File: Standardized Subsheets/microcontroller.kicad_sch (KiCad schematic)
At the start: 62 parts, among them J1 Conn_01x02, J2 Conn_01x02, J3 SWD, SW1 SW_SPDT, U1 STM32F105RCTx, U2 SN65HVD230, U3 SN65HVD230, Y1 16MHz

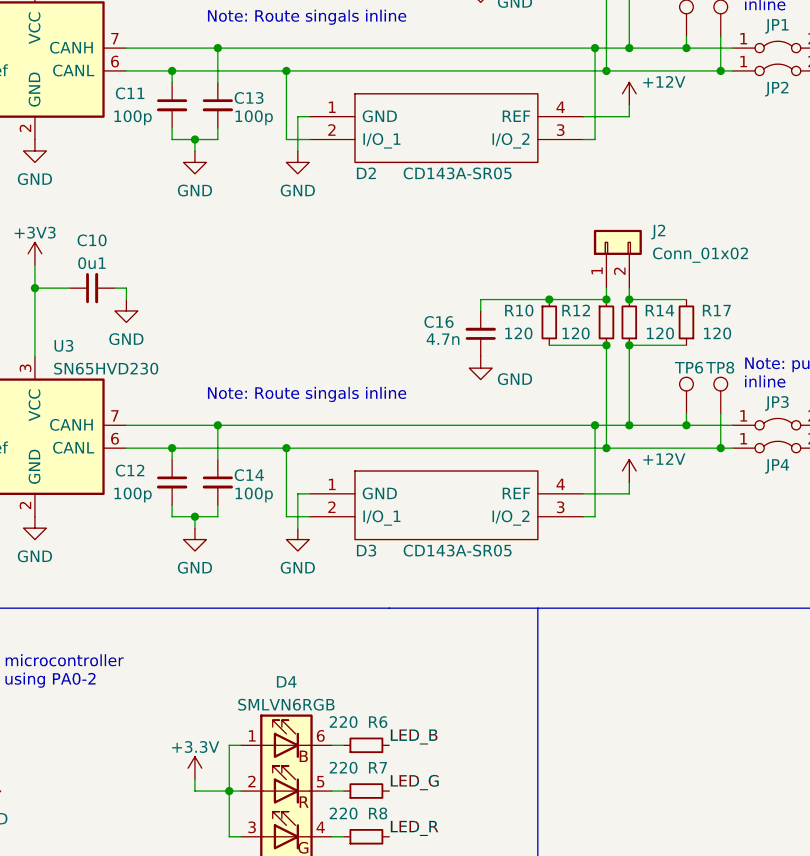
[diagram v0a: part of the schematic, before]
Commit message: updated connector footprint
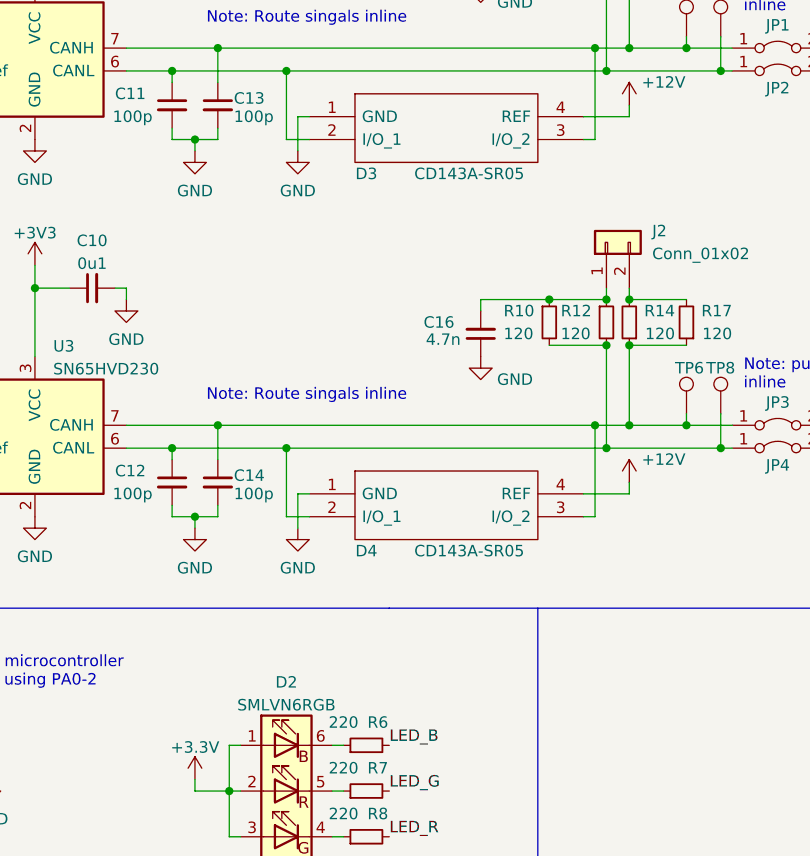
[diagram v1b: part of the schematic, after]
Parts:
- removed D2: CD143A-SR05, CD143ASR05, symbol CD143A-SR05:CD143A-SR05
- added D4: CD143A-SR05, CD143ASR05, symbol CD143A-SR05:CD143A-SR05
- J1, J2: footprint (none) -> Connector_PinHeader_2.54mm:PinHeader_1x02_P2.54mm_Vertical
- renumbered D4 to D2
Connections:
- net +12V: now also D4.4 (REF)
- net GND: now also D4.1 (GND)
- net at C14.1, JP3.1 (A), R14.1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: now also D4.3 (I/O_2); no longer D3.3 (I/O_2)
- net at C13.1, JP1.1 (A), R13.1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: now also D3.3 (I/O_2)
- net at C12.1, JP4.1 (A), R10.2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: now also D4.2 (I/O_1); no longer D3.2 (I/O_1)
- net at C11.1, JP2.1 (A), R11.2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: now also D3.2 (I/O_1)

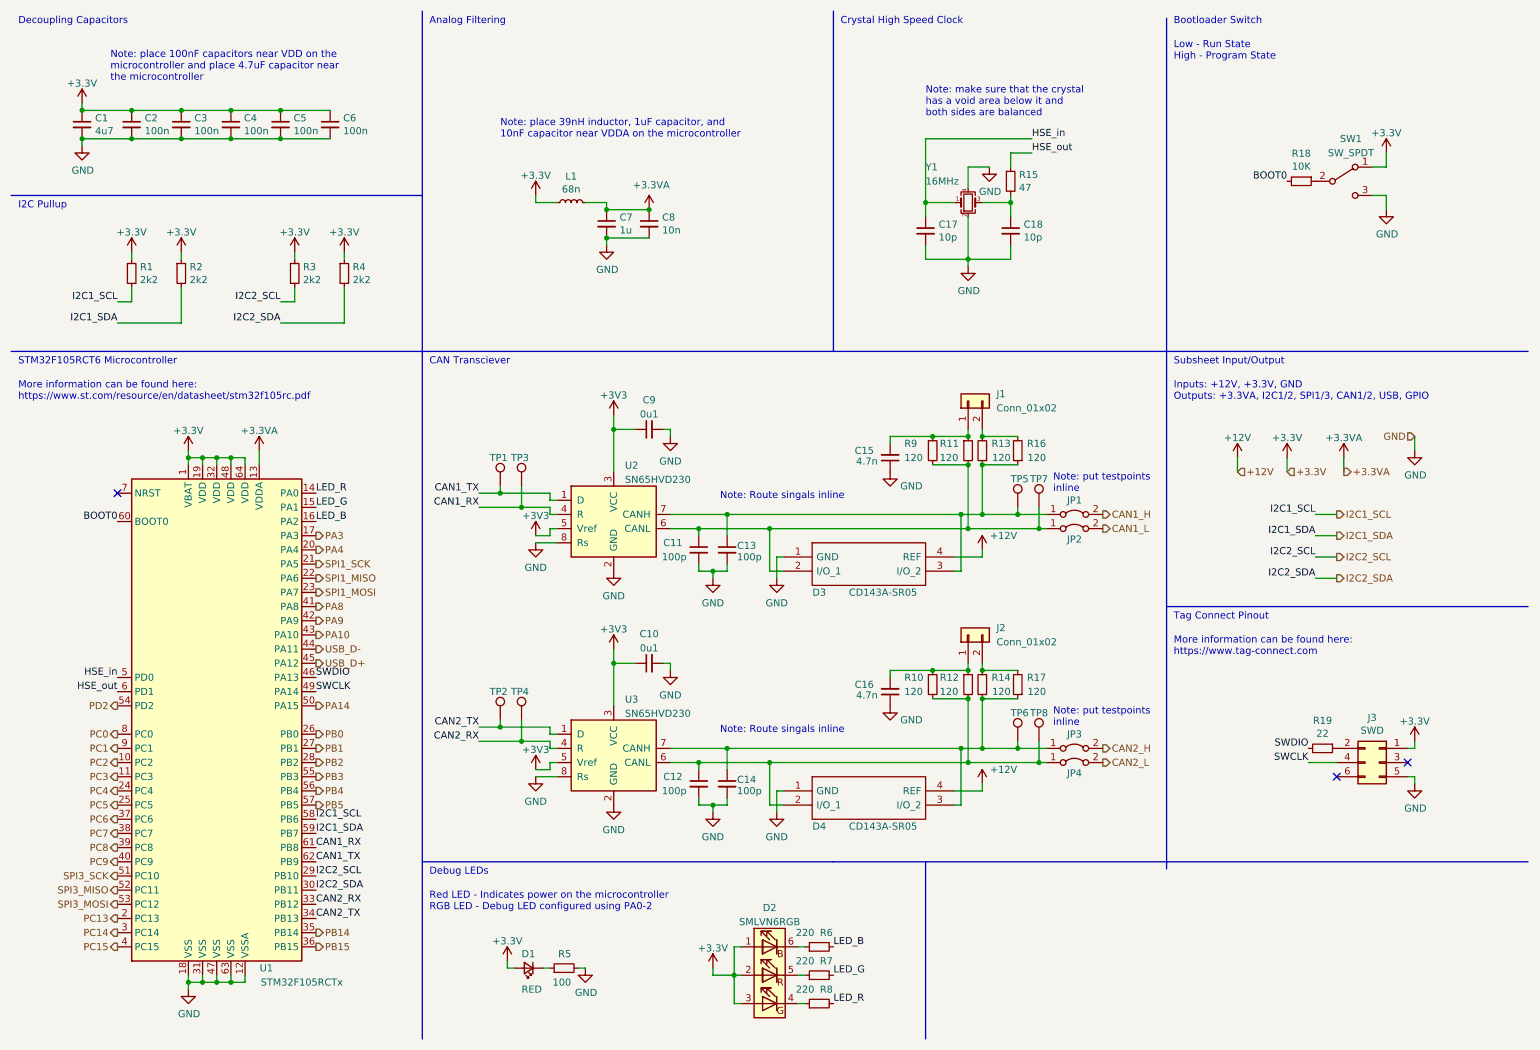
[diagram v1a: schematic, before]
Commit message: Finalized microcontroller schematic
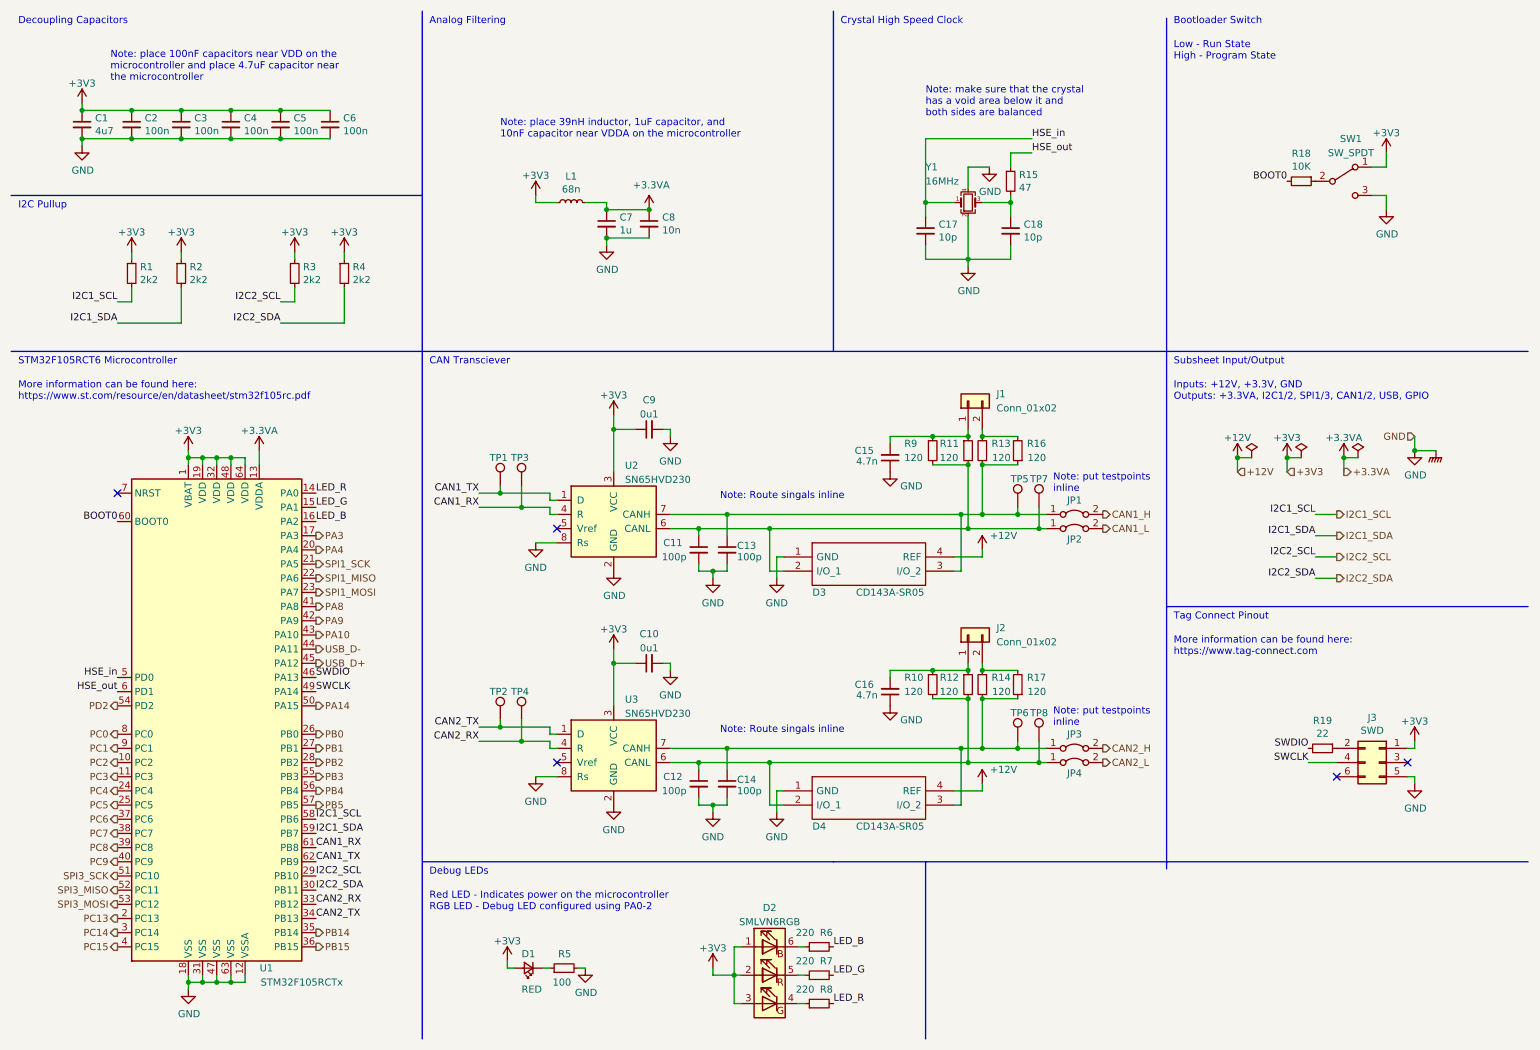
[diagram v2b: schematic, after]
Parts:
- removed D3, D4: CD143A-SR05, CD143ASR05, symbol CD143A-SR05:CD143A-SR05
- added D3, D4: CD143A-SR05, Global Libraries:CD143ASR05, symbol Global Symbols:CD143A-SR05
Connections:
- net +3.3V is gone; now on net +3V3: C1.1, C2.1, C3.1, C4.1, C5.1, C6.1, D1.2 (A), D2.1 (BA), D2.2 (RA), D2.3 (GA), J3.1 (Pin_1), L1.1, R1.1, R2.1, R3.1, R4.1, SW1.1 (A), U1.1 (VBAT), U1.19 (VDD), U1.32 (VDD), U1.48 (VDD), U1.64 (VDD)
- net +12V: now also D3.4 (REF), D4.4 (REF)
- net +3V3: no longer U2.5 (Vref), U3.5 (Vref)
- net GND: now also D3.1 (GND), D4.1 (GND)
- net at C14.1, JP3.1 (A), R14.1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: now also D4.3 (I/O_2)
- net at C13.1, JP1.1 (A), R13.1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: now also D3.3 (I/O_2)
- net at C12.1, JP4.1 (A), R10.2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: now also D4.2 (I/O_1)
- net at C11.1, JP2.1 (A), R11.2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: now also D3.2 (I/O_1)
- no-connect marks 3 -> 5

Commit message: version control
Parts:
- removed D3, D4: CD143A-SR05, Global Libraries:CD143ASR05, symbol Global Symbols:CD143A-SR05
- added U4, U5: CD143A-SR05, Global Libraries:CD143ASR05, symbol Global_Library:CD143A-SR05
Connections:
- net +12V: now also U4.3 (I/O_2), U5.3 (I/O_2)
- net GND: now also U4.1 (GND), U5.1 (GND)
- net at C12.1, JP4.1 (A), R10.2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: now also U5.2 (I/O_1)
- net at C14.1, JP3.1 (A), R14.1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: now also U5.4 (REF)
- net at C13.1, JP1.1 (A), R13.1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: now also U4.4 (REF)
- net at C11.1, JP2.1 (A), R11.2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: now also U4.2 (I/O_1)
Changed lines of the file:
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@@
-    (stroke (width 0) (type default) (color 0 0 0 0))
-  )
-  (wire (pts (xy 148.59 154.94) (xy 151.13 154.94))
     (stroke (width 0) (type default) (color 0 0 0 0))
   )
@@
     (stroke (width 0) (type default) (color 0 0 0 0))
   )
+  (wire (pts (xy 176.53 110.49) (xy 186.69 110.49))
+    (stroke (width 0) (type default) (color 0 0 0 0))
+  )
   (wire (pts (xy 177.8 93.98) (xy 184.15 93.98))
     (stroke (width 0) (type default) (color 0 0 0 0))
@@
     (stroke (width 0) (type default) (color 0 0 0 0))
   )
+  (wire (pts (xy 176.53 113.03) (xy 182.88 113.03))
+    (stroke (width 0) (type default) (color 0 0 0 0))
+  )
   (wire (pts (xy 262.89 149.86) (xy 264.16 149.86))
     (stroke (width 0) (type default) (color 0 0 0 0))
@@
     (stroke (width 0) (type default) (color 0 0 0 0))
   )
-  (wire (pts (xy 181.61 152.4) (xy 186.69 152.4))
+  (wire (pts (xy 176.53 152.4) (xy 186.69 152.4))
     (stroke (width 0) (type default) (color 0 0 0 0))
   )
@@
     (stroke (width 0) (type default) (color 0 0 0 0))
   )
-  (wire (pts (xy 181.61 113.03) (xy 182.88 113.03))
-    (stroke (width 0) (type default) (color 0 0 0 0))
-  )
   (wire (pts (xy 142.24 190.5) (xy 143.51 190.5))
     (stroke (width 0) (type default) (color 0 0 0 0))
@@
     (stroke (width 0) (type default) (color 0 0 0 0))
   )
+  (wire (pts (xy 149.86 110.49) (xy 156.21 110.49))
+    (stroke (width 0) (type default) (color 0 0 0 0))
+  )
   (wire (pts (xy 52.07 30.48) (xy 60.96 30.48))
     (stroke (width 0) (type default) (color 0 0 0 0))
   )
-  (wire (pts (xy 151.13 152.4) (xy 149.86 152.4))
+  (wire (pts (xy 149.86 152.4) (xy 156.21 152.4))
     (stroke (width 0) (type default) (color 0 0 0 0))
   )
@@
     (stroke (width 0) (type default) (color 0 0 0 0))
   )
-  (wire (pts (xy 151.13 110.49) (xy 149.86 110.49))
-    (stroke (width 0) (type default) (color 0 0 0 0))
-  )
   (wire (pts (xy 264.16 144.78) (xy 264.16 143.51))
     (stroke (width 0) (type default) (color 0 0 0 0))
@@
     (stroke (width 0) (type default) (color 0 0 0 0))
   )
+  (wire (pts (xy 148.59 154.94) (xy 156.21 154.94))
+    (stroke (width 0) (type default) (color 0 0 0 0))
+  )
   (wire (pts (xy 140.97 102.87) (xy 140.97 106.68))
     (stroke (width 0) (type default) (color 0 0 0 0))
@@
     (stroke (width 0) (type default) (color 0 0 0 0))
   )
-  (wire (pts (xy 181.61 154.94) (xy 182.88 154.94))
+  (wire (pts (xy 176.53 154.94) (xy 182.88 154.94))
     (stroke (width 0) (type default) (color 0 0 0 0))
   )
@@
     (stroke (width 0) (type default) (color 0 0 0 0))
   )
-  (wire (pts (xy 181.61 110.49) (xy 186.69 110.49))
-    (stroke (width 0) (type default) (color 0 0 0 0))
-  )
   (wire (pts (xy 246.38 114.3) (xy 250.19 114.3))
     (stroke (width 0) (type default) (color 0 0 0 0))
@@
     (stroke (width 0) (type default) (color 0 0 0 0))
   )
-  (wire (pts (xy 148.59 113.03) (xy 151.13 113.03))
-    (stroke (width 0) (type default) (color 0 0 0 0))
-  )
   (wire (pts (xy 177.8 88.9) (xy 184.15 88.9))
     (stroke (width 0) (type default) (color 0 0 0 0))
@@
   )
   (wire (pts (xy 176.53 46.99) (xy 181.61 46.99))
+    (stroke (width 0) (type default) (color 0 0 0 0))
+  )
+  (wire (pts (xy 148.59 113.03) (xy 156.21 113.03))
     (stroke (width 0) (type default) (color 0 0 0 0))
   )
@@
     (pin "2")
   )
-  (symbol (lib_id "Global Symbols:CD143A-SR05") (at 151.13 152.4 0) (unit 1)
-    (in_bom yes) (on_board yes)
-    (property "Reference" "D4" (id 0) (at 157.48 158.75 0))
-    (property "Value" "CD143A-SR05" (id 1) (at 170.18 158.75 0))
-    (property "Footprint" "Global Libraries:CD143ASR05" (id 2) (at 177.8 149.86 0)
-      (effects (font (size 1.27 1.27)) (justify left) hide)
-    )
-    (property "Datasheet" "https://www.bourns.com/docs/Product-Datasheets/CD143A-SR05_12.pdf" (id 3) (at 177.8 152.4 0)
-      (effects (font (size 1.27 1.27)) (justify left) hide)
-    )
-    (property "Description" "TVS Diode Array 500W Vcc,2xData SOT143" (id 4) (at 177.8 154.94 0)
-      (effects (font (size 1.27 1.27)) (justify left) hide)
-    )
-    (property "Height" "1.24" (id 5) (at 177.8 157.48 0)
-      (effects (font (size 1.27 1.27)) (justify left) hide)
-    )
-    (property "Mouser Part Number" "652-CD143A-SR05" (id 6) (at 177.8 160.02 0)
-      (effects (font (size 1.27 1.27)) (justify left) hide)
-    )
-    (property "Mouser Price/Stock" "https://www.mouser.co.uk/ProductDetail/Bourns/CD143A-SR05?qs=tQpxx9W%2FqMmkp6h6iUxcCg%3D%3D" (id 7) (at 177.8 162.56 0)
-      (effects (font (size 1.27 1.27)) (justify left) hide)
-    )
-    (property "Manufacturer_Name" "Bourns" (id 8) (at 177.8 165.1 0)
-      (effects (font (size 1.27 1.27)) (justify left) hide)
-    )
-    (property "Manufacturer_Part_Number" "CD143A-SR05" (id 9) (at 177.8 167.64 0)
-      (effects (font (size 1.27 1.27)) (justify left) hide)
-    )
-    (pin "1")
-    (pin "2")
-    (pin "3")
-    (pin "4")
-  )
   (symbol (lib_id "Jumper:Jumper_2_Bridged") (at 203.2 144.78 0) (unit 1)
     (in_bom yes) (on_board yes)
@@
     (pin "1")
   )
-  (symbol (lib_id "Global Symbols:CD143A-SR05") (at 151.13 110.49 0) (unit 1)
-    (in_bom yes) (on_board yes)
-    (property "Reference" "D3" (id 0) (at 157.48 116.84 0))
-    (property "Value" "CD143A-SR05" (id 1) (at 170.18 116.84 0))
-    (property "Footprint" "Global Libraries:CD143ASR05" (id 2) (at 177.8 107.95 0)
-      (effects (font (size 1.27 1.27)) (justify left) hide)
-    )
-    (property "Datasheet" "https://www.bourns.com/docs/Product-Datasheets/CD143A-SR05_12.pdf" (id 3) (at 177.8 110.49 0)
-      (effects (font (size 1.27 1.27)) (justify left) hide)
-    )
-    (property "Description" "TVS Diode Array 500W Vcc,2xData SOT143" (id 4) (at 177.8 113.03 0)
-      (effects (font (size 1.27 1.27)) (justify left) hide)
-    )
-    (property "Height" "1.24" (id 5) (at 177.8 115.57 0)
-      (effects (font (size 1.27 1.27)) (justify left) hide)
-    )
-    (property "Mouser Part Number" "652-CD143A-SR05" (id 6) (at 177.8 118.11 0)
-      (effects (font (size 1.27 1.27)) (justify left) hide)
-    )
-    (property "Mouser Price/Stock" "https://www.mouser.co.uk/ProductDetail/Bourns/CD143A-SR05?qs=tQpxx9W%2FqMmkp6h6iUxcCg%3D%3D" (id 7) (at 177.8 120.65 0)
-      (effects (font (size 1.27 1.27)) (justify left) hide)
-    )
-    (property "Manufacturer_Name" "Bourns" (id 8) (at 177.8 123.19 0)
-      (effects (font (size 1.27 1.27)) (justify left) hide)
-    )
-    (property "Manufacturer_Part_Number" "CD143A-SR05" (id 9) (at 177.8 125.73 0)
-      (effects (font (size 1.27 1.27)) (justify left) hide)
-    )
-    (pin "1")
-    (pin "2")
-    (pin "3")
-    (pin "4")
-  )
   (symbol (lib_id "power:PWR_FLAG") (at 254 92.71 0) (unit 1)
     (in_bom yes) (on_board yes) (fields_autoplaced)
@@
     (pin "2")
   )
+  (symbol (lib_id "Global_Library:CD143A-SR05") (at 166.37 153.035 0) (unit 1)
+    (in_bom yes) (on_board yes)
+    (property "Reference" "U5" (id 0) (at 166.37 158.7531 0))
+    (property "Value" "CD143A-SR05" (id 1) (at 166.37 161.29 0))
+    (property "Footprint" "Global Libraries:CD143ASR05" (id 2) (at 166.37 153.035 0)
+      (effects (font (size 1.27 1.27)) hide)
+    )
+    (property "Datasheet" "" (id 3) (at 166.37 153.035 0)
+      (effects (font (size 1.27 1.27)) hide)
+    )
+    (pin "1")
+    (pin "2")
+    (pin "3")
+    (pin "4")
+  )
   (symbol (lib_id "power:GND") (at 130.81 130.81 0) (unit 1)
     (in_bom yes) (on_board yes) (fields_autoplaced)
@@
     (pin "1")
     (pin "2")
+  )
+  (symbol (lib_id "Global_Library:CD143A-SR05") (at 166.37 111.125 0) (unit 1)
+    (in_bom yes) (on_board yes)
+    (property "Reference" "U4" (id 0) (at 166.37 116.8431 0))
+    (property "Value" "CD143A-SR05" (id 1) (at 166.37 119.38 0))
+    (property "Footprint" "Global Libraries:CD143ASR05" (id 2) (at 166.37 111.125 0)
+      (effects (font (size 1.27 1.27)) hide)
+    )
+    (property "Datasheet" "" (id 3) (at 166.37 111.125 0)
+      (effects (font (size 1.27 1.27)) hide)
+    )
+    (pin "1")
+    (pin "2")
+    (pin "3")
+    (pin "4")
   )
   (symbol (lib_id "Device:C_Small") (at 127 129.54 90) (unit 1)
@@
       (reference "D2") (unit 1) (value "SMLVN6RGB") (footprint "LED_SMD:LED_ROHM_SMLVN6")
     )
-    (path "/2cd9c368-7cf6-4436-8f97-8df5e0c4c88a"
-      (reference "D3") (unit 1) (value "CD143A-SR05") (footprint "Global Libraries:CD143ASR05")
-    )
-    (path "/012bc234-b892-4c9c-8d8e-269a7d61ad48"
-      (reference "D4") (unit 1) (value "CD143A-SR05") (footprint "Global Libraries:CD143ASR05")
-    )
     (path "/27fec5df-f50a-420e-8f18-082a387b0bca"
       (reference "J1") (unit 1) (value "Conn_01x02") (footprint "Connector_PinHeader_2.54mm:PinHeader_1x02_P2.54mm_Vertical")
@@
       (reference "U3") (unit 1) (value "SN65HVD230") (footprint "Package_SO:SOIC-8_3.9x4.9mm_P1.27mm")
     )
+    (path "/5a5b6b3d-5ffb-4ce4-aa28-2da0efdcb609"
+      (reference "U4") (unit 1) (value "CD143A-SR05") (footprint "Global Libraries:CD143ASR05")
+    )
+    (path "/48254f4e-24c7-449f-9b1f-032c839c6de7"
+      (reference "U5") (unit 1) (value "CD143A-SR05") (footprint "Global Libraries:CD143ASR05")
+    )
     (path "/00000000-0000-0000-0000-000063457466"

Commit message: updated microcontroller
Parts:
- removed C11, C12, C13, C14: 100p, Capacitor_SMD:C_0603_1608Metric, symbol Device:C_Small
- removed U4, U5: CD143A-SR05, Global Libraries:CD143ASR05, symbol Global_Library:CD143A-SR05
- added D?: DT1446-04TS-7, Global Libraries:SOT95P280X100-6N, symbol Global_Library:DT1446-04TS-7
- renumbered J1 to J3, J2 to J4, J3 to J5
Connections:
- net GND: now also D?.2 (VSS)
- net at JP3.1 (A), R14.1, R17.1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: now also D?.3 (I/O2)
- net at JP1.1 (A), R13.1, R16.1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: now also D?.6 (I/O4)
- net at JP4.1 (A), R10.2, R12.2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: now also D?.1 (I/O1)
- net at JP2.1 (A), R11.2, R9.2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: now also D?.4 (I/O3)
- new net +5V: D?.5 (VCC)
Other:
- note added: "Inputs: +5V, +3.3V, GND Outputs: +3.3VA, I2C1/2, SPI1/3, CAN1/2, USB, GPIO"
- note removed: "Inputs: +12V, +3.3V, GND Outputs: +3.3VA, I2C1/2, SPI1/3, CAN1/2, USB, GPIO"
- moved on the sheet: C15, C16, J3, J4, JP1, JP2, JP3, JP4, R10, R11, R12, R13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

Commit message: gitignore
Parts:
- gave numbers to parts that had none: 1
- renumbered C15 to C11, C16 to C12, C17 to C13, C18 to C14, D2 to D3, R9 to R10, R10 to R11, R11 to R12, R12 to R13, R13 to R14, R14 to R15, R15 to R18, R18 to R19, R1 to R2, R19 to R20, R2 to R3, R3 to R4, R4 to R5, R5 to R6, R6 to R7, R7 to R8, R8 to R9

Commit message: Probably will be breaking everything
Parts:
- renumbered C2 to C10, C3 to C11, C4 to C12, C5 to C13, C6 to C14, C7 to C15, C8 to C16, C9 to C17, C10 to C18, C11 to C19, C12 to C20, C13 to C21, C14 to C22, C1 to C9, D3 to D10, D1 to D8, D2 to D9, J3 to J4, J4 to J5, J5 to J6, L1 to L2, R6 to R10, R7 to R11, R8 to R12, R9 to R13, R10 to R14, R11 to R15, R12 to R16, R13 to R17, R14 to R18, R15 to R19, R16 to R20, R17 to R21, R18 to R22, R19 to R23, R20 to R24, R2 to R6, R3 to R7, R4 to R8, R5 to R9, SW1 to SW3, U1 to U3, U2 to U4, U3 to U5
